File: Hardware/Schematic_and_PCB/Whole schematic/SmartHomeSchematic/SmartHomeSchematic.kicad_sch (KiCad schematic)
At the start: 52 parts, among them J1 PIR_sensor, J2 LCD_display, J3 Power, Q1 BC557, Q3 BC557, Q4 BC557, Q5 BC557, Q6 BC557, Q7 BC557, SW1 Room_1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

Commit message: Replace arduino nano every symbol with new symbol and add resistor values.
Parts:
- removed A1: Arduino_Nano_Every, Module:Arduino_Nano, symbol MCU_Module:Arduino_Nano_Every
- added A2: Arduino_Nano_Every, Module:Arduino_Nano, symbol arduino_nano_every_custom:Arduino_Nano_Every
- R10, R11, R15, R16, R24, R25, R4, R5: value ? -> 450
- R14, R23, R3, R9: value ? -> 650
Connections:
- net +5V: now also A2.27 (+5V)
- net +9V: now also A2.30 (VIN)
- net GND: now also A2.29 (GND), A2.4 (GND)
- net blue led room 3: now also A2.9 (D6)
- net button back: now also A2.15 (D12)
- net button down: now also A2.11 (D8)
- net button ok: now also A2.14 (D11)
- net button up: now also A2.10 (D7)
- net control panel pot: now also A2.19 (A0)
- net green led room 3: now also A2.8 (D5)
- net lcd SCL: now also A2.24 (SCL/A5)
- net lcd SDA: now also A2.23 (SDA/A4)
- net led door: now also A2.13 (D10)
- net led room 1: now also A2.12 (D9)
- net led room 2: now also A2.5 (D2)
- net red led room 3: now also A2.6 (D3)
- net at SW1.1: now also A2.25 (A6)
- net at RV2.2: now also A2.21 (A2)
- net at SW4.2: now also A2.7 (D4)
- net at SW2.2: now also A2.1 (D0)
- net at R26.1: now also A2.22 (A3)
- net at J1.2 (Pin_2): now also A2.16 (D13)
- net at SW3.2: now also A2.2 (D1)
- net at RV1.2: now also A2.20 (A1)
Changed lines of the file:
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@@
 			)
 		)
-		(property "Value" "?"
+		(property "Value" "450"
 			(at 315.976 156.718 90)
 			(effects
@@
 	)
 	(symbol
+		(lib_id "arduino_nano_every_custom:Arduino_Nano_Every")
+		(at 123.19 82.55 0)
+		(unit 1)
+		(exclude_from_sim no)
+		(in_bom yes)
+		(on_board yes)
+		(dnp no)
+		(fields_autoplaced yes)
+		(property "Reference" "A2"
+			(at 125.3841 107.95 0)
+			(effects
+				(font
+					(size 1.27 1.27)
+				)
+				(justify left)
+			)
+		)
+		(property "Value" "Arduino_Nano_Every"
+			(at 125.3841 110.49 0)
+			(effects
+				(font
+					(size 1.27 1.27)
+				)
+				(justify left)
+			)
+		)
+		(property "Footprint" "Module:Arduino_Nano"
+			(at 123.19 82.55 0)
+			(effects
+				(font
+					(size 1.27 1.27)
+					(italic yes)
+				)
+				(hide yes)
+			)
+		)
+		(property "Datasheet" "https://content.arduino.cc/assets/NANOEveryV3.0_sch.pdf"
+			(at 123.19 82.55 0)
+			(effects
+				(font
+					(size 1.27 1.27)
+				)
+				(hide yes)
+			)
+		)
+		(property "Description" "Arduino Nano Every"
+			(at 123.19 82.55 0)
+			(effects
+				(font
+					(size 1.27 1.27)
+				)
+				(hide yes)
+			)
+		)
+		(pin "13"
+		)
+		(pin "21"
+		)
+		(pin "24"
+		)
+		(pin "16"
+		)
+		(pin "28"
+		)
+		(pin "26"
+		)
+		(pin "18"
+		)
+		(pin "15"
+		)
+		(pin "25"
+		)
+		(pin "14"
+		)
+		(pin "6"
+		)
+		(pin "27"
+		)
+		(pin "10"
+		)
+		(pin "3"
+		)
+		(pin "4"
+		)
+		(pin "7"
+		)
+		(pin "8"
+		)
+		(pin "11"
+		)
+		(pin "19"
+		)
+		(pin "23"
+		)
+		(pin "5"
+		)
+		(pin "1"
+		)
+		(pin "2"
+		)
+		(pin "30"
+		)
+		(pin "12"
+		)
+		(pin "29"
+		)
+		(pin "20"
+		)
+		(pin "22"
+		)
+		(pin "9"
+		)
+		(pin "17"
+		)
+		(instances
+			(project ""
+				(path "/11858cf2-bd6b-4d20-a6d0-cbf7ff297707"
+					(reference "A2")
+					(unit 1)
+				)
+			)
+		)
+	)
+	(symbol
 		(lib_id "power:+5V")
 		(at 130.81 229.87 0)
@@
 			)
 		)
-		(property "Value" "?"
+		(property "Value" "450"
 			(at 315.976 80.518 90)
 			(effects
@@
 			)
 		)
-		(property "Value" "?"
+		(property "Value" "450"
 			(at 315.976 85.598 90)
 			(effects
@@
 			)
 		)
-		(property "Value" "?"
+		(property "Value" "450"
 			(at 315.976 151.638 90)
 			(effects
@@
 			)
 		)
-		(property "Value" "?"
+		(property "Value" "650"
 			(at 316.23 110.998 90)
 			(effects
@@
 			)
 		)
-		(property "Value" "?"
+		(property "Value" "450"
 			(at 315.976 193.548 90)
 			(effects
@@
 			)
 		)
-		(property "Value" "?"
+		(property "Value" "450"
 			(at 315.976 116.078 90)
 			(effects
@@
 			)
 		)
-		(property "Value" "?"
+		(property "Value" "650"
 			(at 316.23 183.388 90)
 			(effects
@@
 			)
 		)
-		(property "Value" "?"
+		(property "Value" "650"
 			(at 316.23 146.558 90)
 			(effects
@@
 	)
 	(symbol
-		(lib_id "MCU_Module:Arduino_Nano_Every")
-		(at 123.19 82.55 0)
-		(unit 1)
-		(exclude_from_sim no)
-		(in_bom yes)
-		(on_board yes)
-		(dnp no)
-		(property "Reference" "A1"
-			(at 131.064 58.674 0)
-			(effects
-				(font
-					(size 1.27 1.27)
-				)
-				(justify left)
-			)
-		)
-		(property "Value" "Arduino_Nano_Every"
-			(at 125.476 106.68 0)
-			(effects
-				(font
-					(size 1.27 1.27)
-				)
-				(justify left)
-			)
-		)
-		(property "Footprint" "Module:Arduino_Nano"
-			(at 123.19 82.55 0)
-			(effects
-				(font
-					(size 1.27 1.27)
-					(italic yes)
-				)
-				(hide yes)
-			)
-		)
-		(property "Datasheet" "https://content.arduino.cc/assets/NANOEveryV3.0_sch.pdf"
-			(at 123.19 82.55 0)
-			(effects
-				(font
-					(size 1.27 1.27)
-				)
-				(hide yes)
-			)
-		)
-		(property "Description" "Arduino Nano Every"
-			(at 123.19 82.55 0)
-			(effects
-				(font
-					(size 1.27 1.27)
-				)
-				(hide yes)
-			)
-		)
-		(pin "2"
-		)
-		(pin "6"
-		)
-		(pin "19"
-		)
-		(pin "26"
-		)
-		(pin "29"
-		)
-		(pin "25"
-		)
-		(pin "12"
-		)
-		(pin "14"
-		)
-		(pin "15"
-		)
-		(pin "17"
-		)
-		(pin "13"
-		)
-		(pin "3"
-		)
-		(pin "28"
-		)
-		(pin "30"
-		)
-		(pin "23"
-		)
-		(pin "8"
-		)
-		(pin "21"
-		)
-		(pin "22"
-		)
-		(pin "5"
-		)
-		(pin "20"
-		)
-		(pin "27"
-		)
-		(pin "4"
-		)
-		(pin "18"
-		)
-		(pin "1"
-		)
-		(pin "10"
-		)
-		(pin "24"
-		)
-		(pin "11"
-		)
-		(pin "7"
-		)
-		(pin "16"
-		)
-		(pin "9"
-		)
-		(instances
-			(project ""
-				(path "/11858cf2-bd6b-4d20-a6d0-cbf7ff297707"
-					(reference "A1")
-					(unit 1)
-				)
-			)
-		)
-	)
-	(symbol
 		(lib_id "Device:R")
 		(at 288.29 110.49 90)
@@
 			)
 		)
-		(property "Value" "?"
+		(property "Value" "450"
 			(at 315.976 121.158 90)
 			(effects
@@
 			)
 		)
-		(property "Value" "?"
+		(property "Value" "650"
 			(at 316.23 75.438 90)
 			(effects
@@
 			)
 		)
-		(property "Value" "?"
+		(property "Value" "450"
 			(at 315.976 188.468 90)
 			(effects

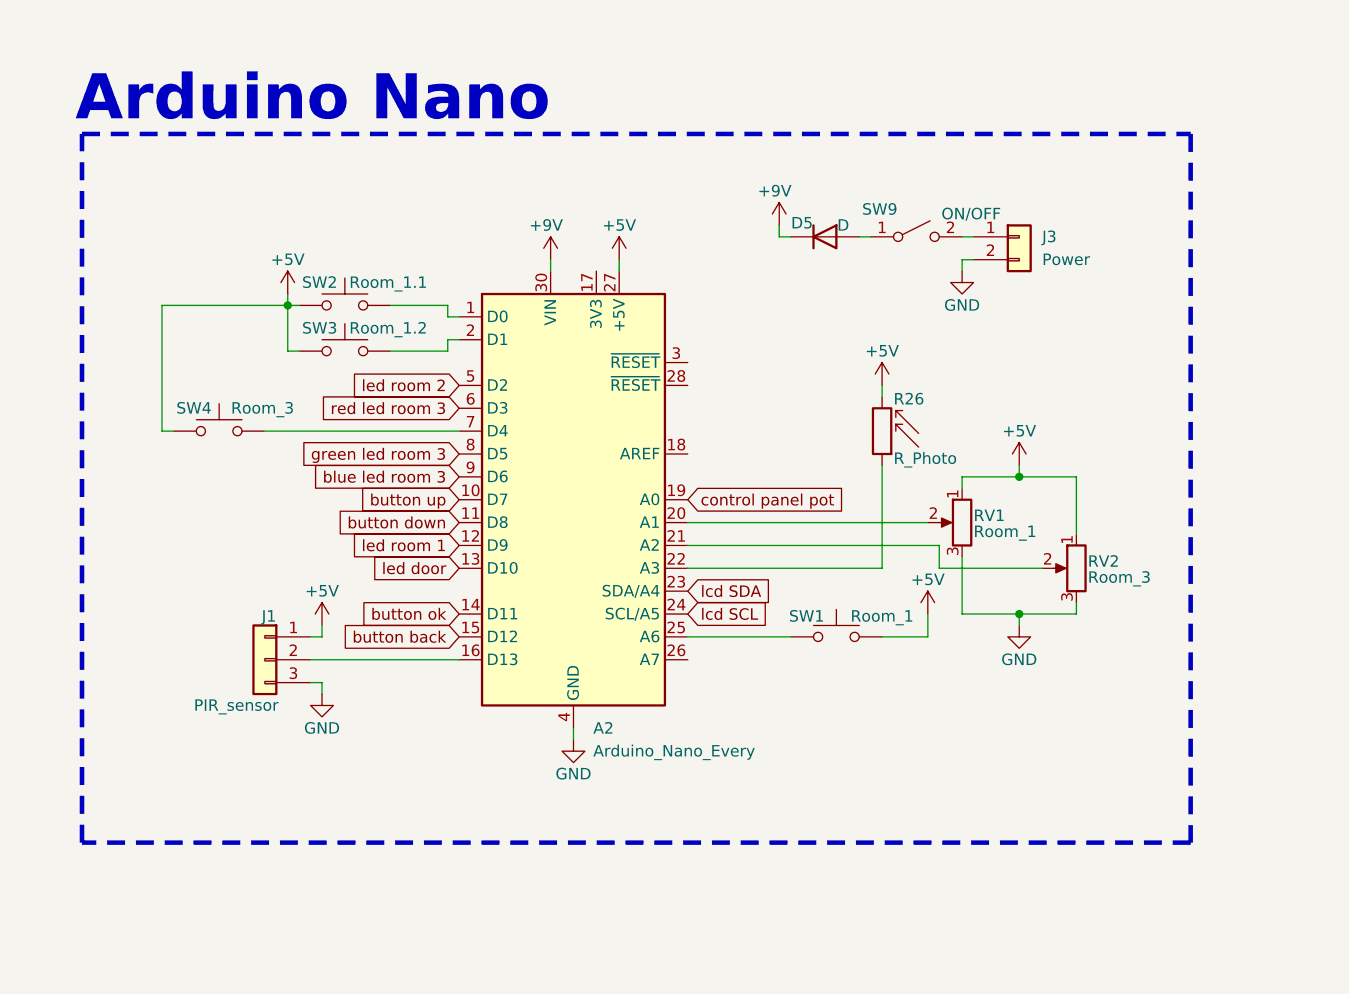
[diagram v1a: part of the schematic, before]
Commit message: Change schematic as was agreed on a meeting, also change  used pins.md.
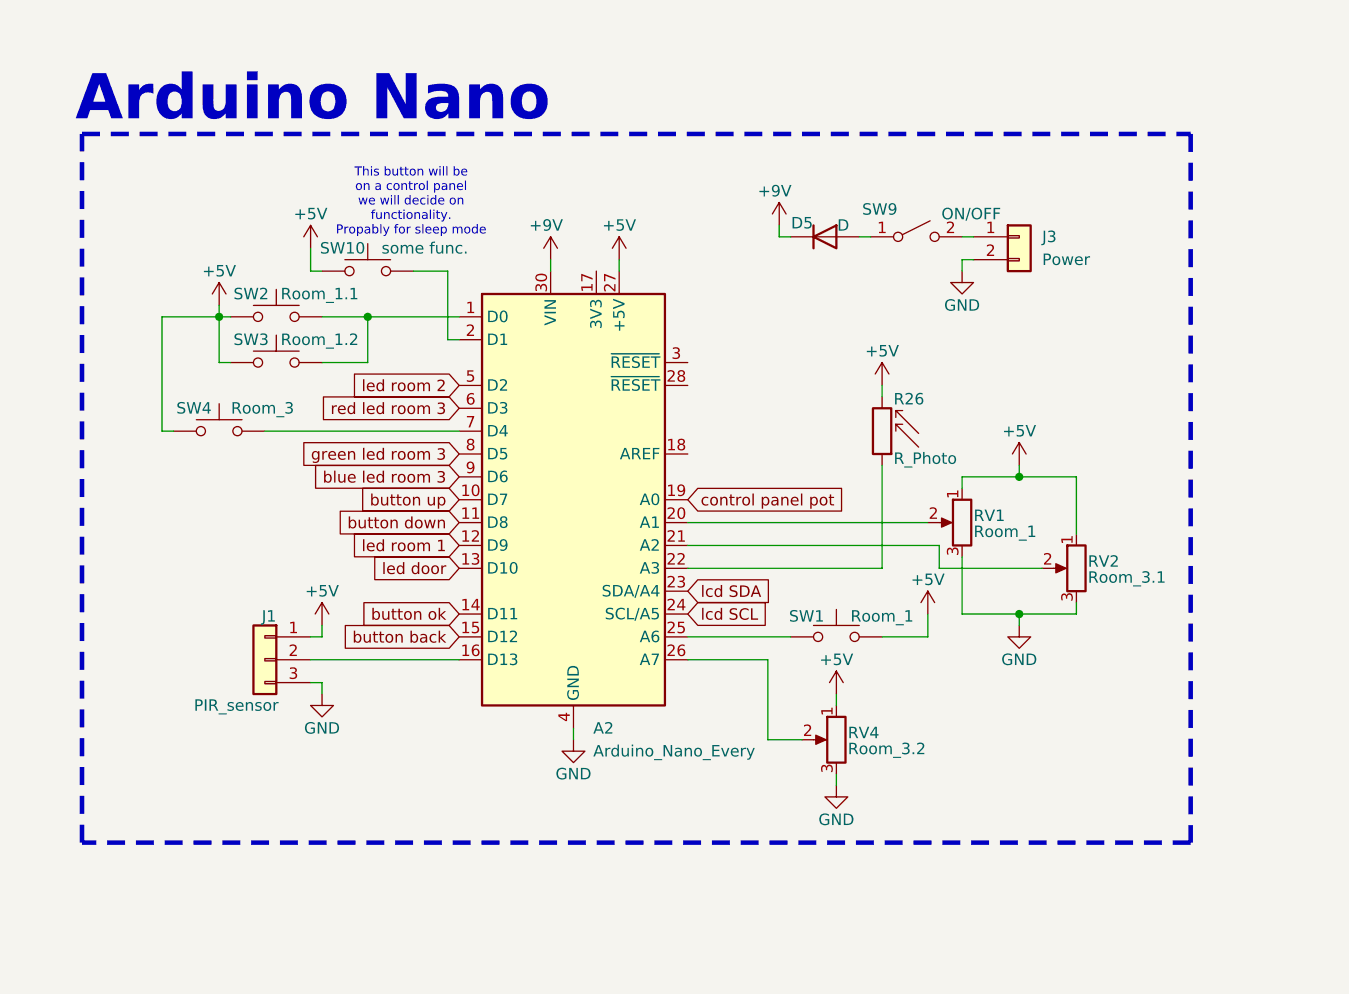
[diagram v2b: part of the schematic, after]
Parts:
- added RV4: Room_3.2, symbol Device:R_Potentiometer
- added SW10: some func., symbol Switch:SW_Push
- RV2: value Room_3 -> Room_3.1
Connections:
- net +5V: now also RV4.1, SW10.1
- net GND: now also RV4.3
- net at A2.1 (D0), SW2.2: now also SW3.2
- net at A2.2 (D1): now also SW10.2; no longer SW3.2
- net at A2.26 (A7): now also RV4.2
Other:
- note added: "This button will be on a control panel we will decide on functionality. Propably for sleep mode"
- moved on the sheet: SW2, SW3

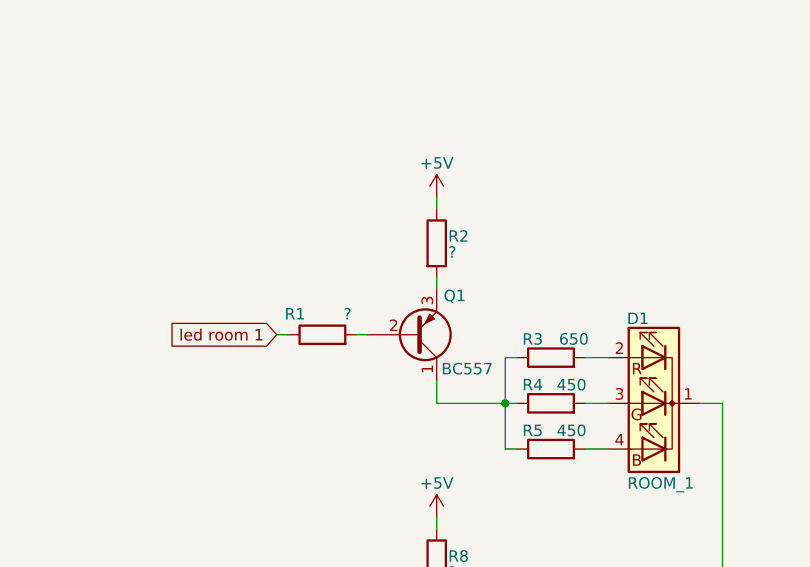
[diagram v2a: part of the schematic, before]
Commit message: Update resistor values.
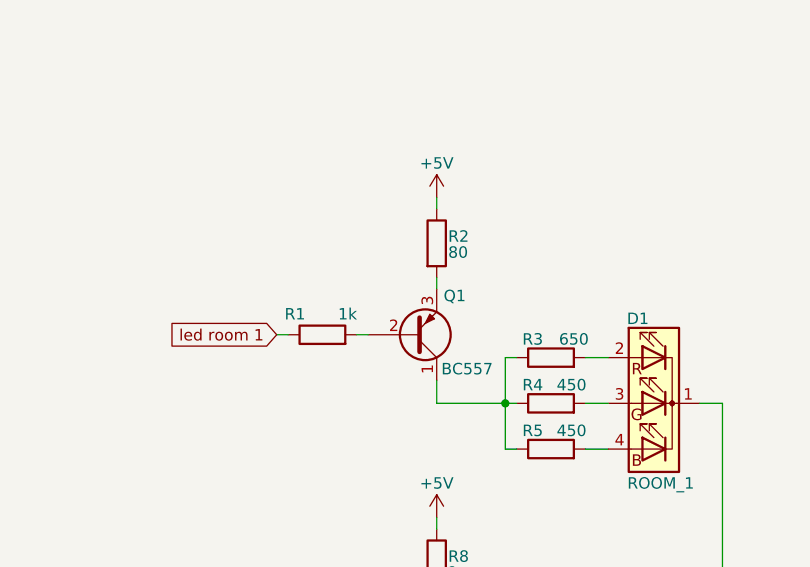
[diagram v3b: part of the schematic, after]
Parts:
- R1: value ? -> 1k
- R2: value ? -> 80
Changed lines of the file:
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@@
 			)
 		)
-		(property "Value" "?"
+		(property "Value" "1k"
 			(at 291.084 72.644 90)
 			(effects
@@
 			)
 		)
-		(property "Value" "?"
+		(property "Value" "80"
 			(at 302.26 65.786 0)
 			(effects

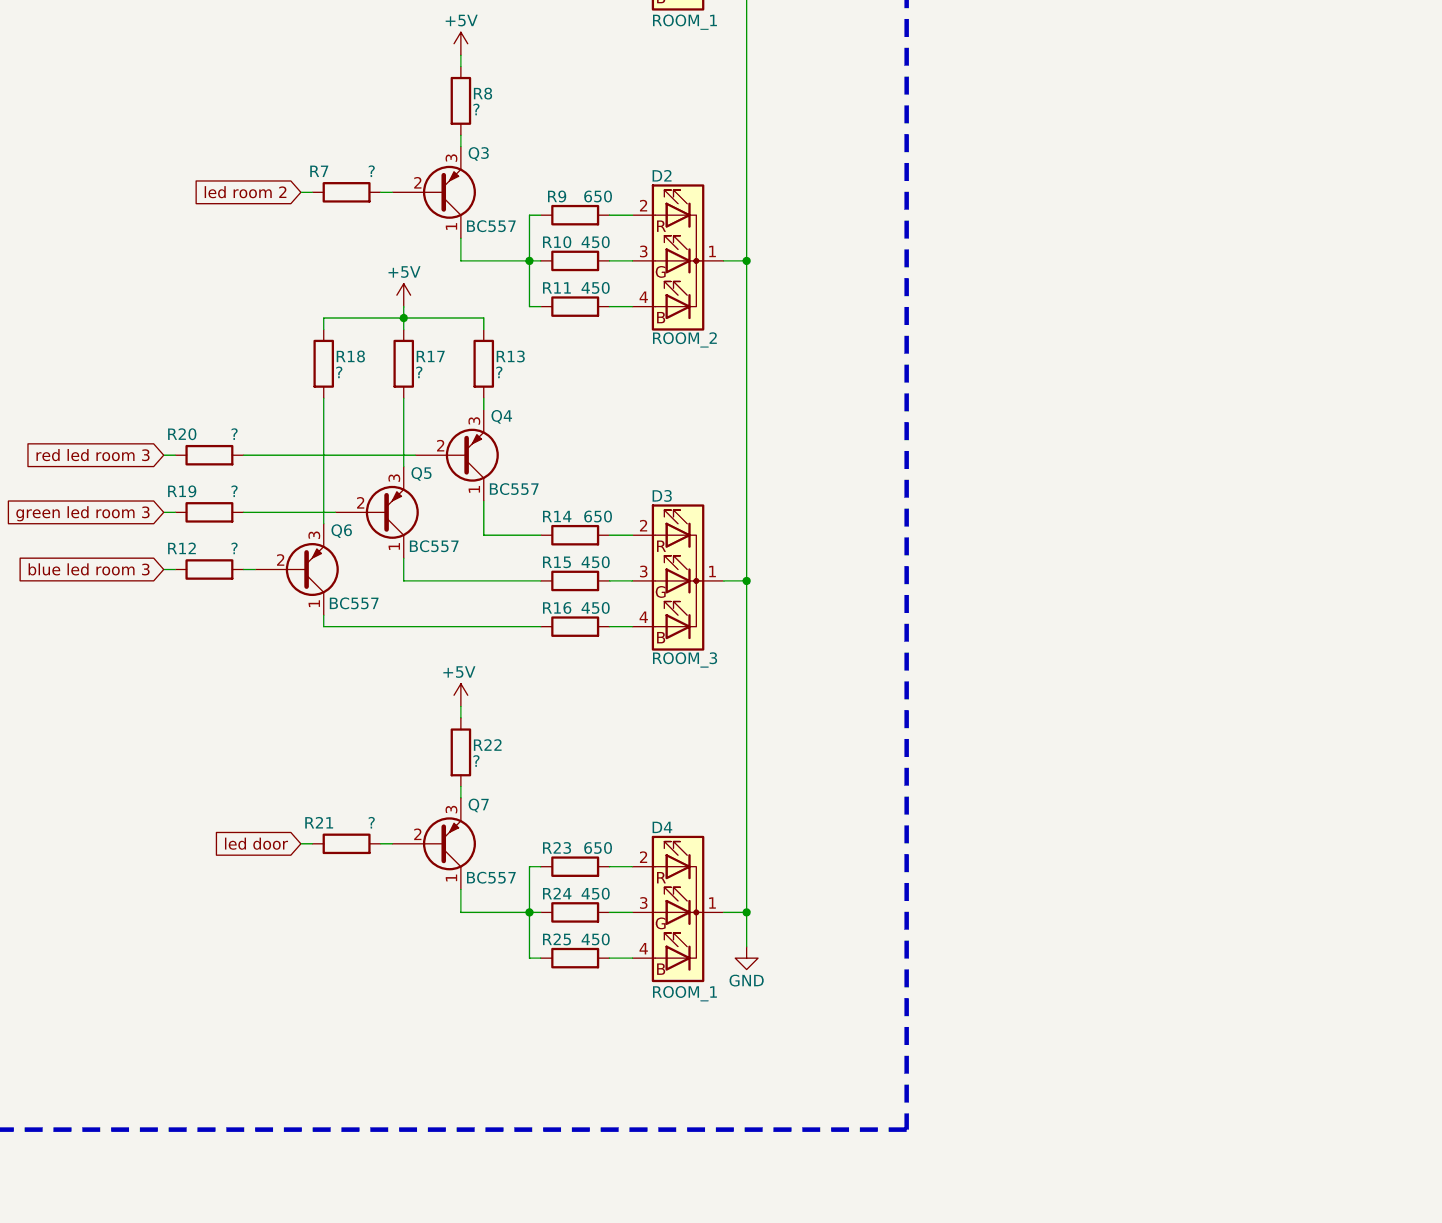
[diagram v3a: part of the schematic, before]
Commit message: Update smarthome schematic with calculations
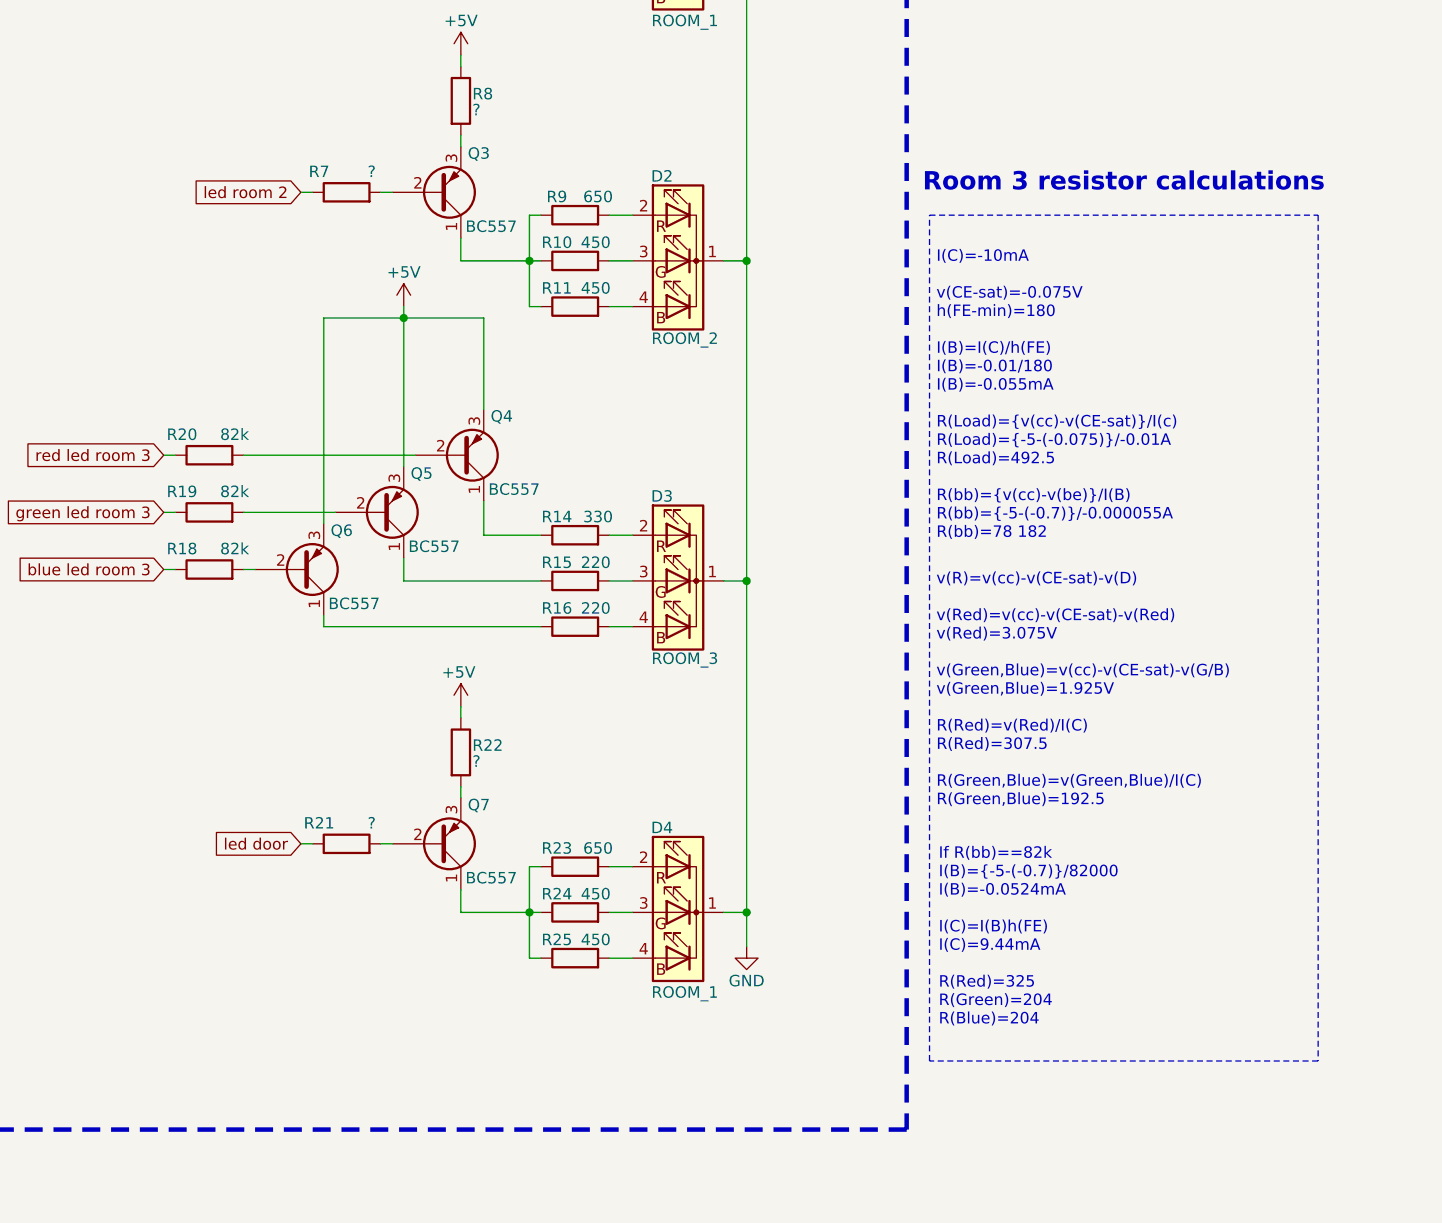
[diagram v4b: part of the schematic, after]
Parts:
- removed R13, R17, R18: ?, symbol Device:R
- R14: value 650 -> 330
- R15, R16: value 450 -> 220
- R18: renamed from R12; value ? -> 82k
- R19, R20: value ? -> 82k
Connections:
- net +5V: now also Q4.3 (E), Q5.3 (E), Q6.3 (E)
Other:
- note added: "I(C)=-10mA v(CE-sat)=-0.075V h(FE-min)=180 I(B)=I(C)/h(FE) I(B)=-0.01/180 I(B)=-0.055mA R(Load)={v(cc)-v(CE-sat)}/I(c) R(Load)={-5-(-0.075)}/-0.01A R(Load)=492.5 R(bb)={v(cc)-v(be)}/I(B) R(bb)={-5-(-0.7)}/-0.000055A R(bb)=78 182"
- note added: "If R(bb)==82k I(B)={-5-(-0.7)}/82000 I(B)=-0.0524mA I(C)=I(B)h(FE) I(C)=9.44mA R(Red)=325 R(Green)=204 R(Blue)=204"
- note added: "Room 3 resistor calculations"
- note added: "v(R)=v(cc)-v(CE-sat)-v(D) v(Red)=v(cc)-v(CE-sat)-v(Red) v(Red)=3.075V v(Green,Blue)=v(cc)-v(CE-sat)-v(G/B) v(Green,Blue)=1.925V R(Red)=v(Red)/I(C) R(Red)=307.5 R(Green,Blue)=v(Green,Blue)/I(C) R(Green,Blue)=192.5"
